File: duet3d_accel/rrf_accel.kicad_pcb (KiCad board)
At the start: 2 copper layers, 118.7 x 50.3 mm, 13 parts, among them J1 Conn_02x05_Odd_Even, U1 LIS3DH

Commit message: Layout in progress.
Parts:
- U1: footprint Package_LGA:LGA-16_3x3mm_P0.5mm_LayoutBorder3x5y -> duet3d_accel:LGA-16_3x3mm_P0.5mm_LayoutBorder3x5y
- moved R4 11.8 mm to (103.8, 99.3)
- moved R6 11.7 mm to (96.1, 99.4)
- moved D1 11.6 mm to (107.1, 100.1)
- moved R5 11.4 mm to (105.9, 99.4)
- moved J1 11.1 mm to (100.0, 93.3)
- moved U1 11.0 mm to (100.0, 100.0)
- moved R1 10.9 mm to (95.1, 99.3)
- moved R3 10.8 mm to (105.2, 101.3)
- moved R2 10.8 mm to (104.8, 99.4)
- moved C2 10.8 mm to (102.4, 100.7)
- moved C3 10.7 mm to (93.8, 99.9)
- moved C1 10.7 mm to (92.2, 99.9)
- moved C4 10.5 mm to (97.3, 99.9)
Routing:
- net /MOSI: track 22.4 -> 26.0 mm
- net Net-(U1-SDA/SDI/SDO): track 6.61 -> 3.88 mm
- net +3V3: track 23.5 -> 25.2 mm
- net Net-(U1-CS): track 2.79 -> 4.40 mm
- net Net-(U1-SCL/SPC): track 6.54 -> 5.48 mm
- net /SCK: track 5.43 -> 4.53 mm
- net Net-(D1-A): track 2.32 -> 1.47 mm
- net /CS: track 14.1 -> 14.8 mm
- net /INT: track 15.0 -> 14.5 mm
- net GNDD: track 16.6 -> 16.4 mm, vias 9 -> 8
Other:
- board size 118.7 x 50.3 mm -> 100 x 100 mm

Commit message: More layout.
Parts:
- moved C1 138.3 mm to (-7.76, 4.40)
- moved C2 138.3 mm to (2.43, 5.19)
- moved C3 138.3 mm to (-6.23, 4.40)
- moved C4 138.3 mm to (-2.65, 4.40)
- moved D1 138.3 mm to (7.13, 4.55)
- moved J1 138.3 mm to (0.00, -2.20)
- moved R1 138.3 mm to (-4.94, 3.84)
- moved R2 138.3 mm to (4.84, 3.87)
- moved R3 138.3 mm to (5.22, 5.82)
- moved R4 138.3 mm to (3.83, 3.84)
- moved R5 138.3 mm to (5.86, 3.87)
- moved R6 138.3 mm to (-3.92, 3.86)
- moved U1 138.3 mm to (0.00, 4.50)
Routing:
- net /MOSI: track 26.0 -> 28.2 mm
- net /SCK: track 4.53 -> 3.49 mm
- net /CS: track 14.8 -> 15.8 mm
- net /MISO: track 5.99 -> 5.06 mm
- net /INT: track 14.5 -> 15.2 mm
- net GNDD: track 16.4 -> 15.8 mm
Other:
- board text added: "1"
- board text added: "LIS3DH"

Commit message: Tweaked the layout
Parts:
- moved C4 0.35 mm to (-3.00, 4.40)
- moved R6 0.30 mm to (-4.22, 3.86)
- moved R1 0.25 mm to (-5.18, 3.86)
- moved C1 0.17 mm to (-7.92, 4.40)
- moved C3 0.17 mm to (-6.40, 4.40)
- moved C2 0.16 mm to (2.59, 5.18)
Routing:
- net +3V3: track 25.3 -> 28.8 mm
- net /CS: track 15.8 -> 14.7 mm
- net GNDD: track 15.8 -> 14.9 mm, vias 8 -> 5
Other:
- outline, holes or cut-outs redrawn

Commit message: Renamed libraries
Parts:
- J1: footprint duet3d_accel:PinHeader_2x05_P2.54mm_Vertical_SMD -> rrf_accel:PinHeader_2x05_P2.54mm_Vertical_SMD
- U1: footprint duet3d_accel:LGA-16_3x3mm_P0.5mm_LayoutBorder3x5y -> rrf_accel:LGA-16_3x3mm_P0.5mm_LayoutBorder3x5y
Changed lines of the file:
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@@
     )
   )
-  (footprint "duet3d_accel:PinHeader_2x05_P2.54mm_Vertical_SMD" (layer "F.Cu")
+  (footprint "rrf_accel:PinHeader_2x05_P2.54mm_Vertical_SMD" (layer "F.Cu")
     (at 0 -2.2 -90)
     (descr "surface-mounted straight pin header, 2x05, 2.54mm pitch, double rows")
@@
     (property "ki_description" "Generic connector, double row, 02x05, odd/even pin numbering scheme (row 1 odd numbers, row 2 even numbers), script generated (kicad-library-utils/schlib/autogen/connector/)")
     (property "ki_keywords" "connector")
-    (fp_text reference "J1" (at 0 -7.41 90) (layer "F.SilkS") hide
-        (effects (font (size 1 1) (thickness 0.15)))
-    )
-    (fp_text value "Conn_02x05_Odd_Even" (at 0 7.41 90) (layer "F.Fab") hide
+    (fp_text reference "J1" (at 0 -7.41 -90) (layer "F.SilkS") hide
+        (effects (font (size 1 1) (thickness 0.15)))
+    )
+    (fp_text value "Conn_02x05_Odd_Even" (at 0 7.41 -90) (layer "F.Fab") hide
         (effects (font (size 1 1) (thickness 0.15)))
     )
@@
     )
   )
-  (footprint "duet3d_accel:LGA-16_3x3mm_P0.5mm_LayoutBorder3x5y" (layer "F.Cu")
+  (footprint "rrf_accel:LGA-16_3x3mm_P0.5mm_LayoutBorder3x5y" (layer "F.Cu")
     (at 0 4.5 180)
     (descr "LGA, 16 Pin (http://www.st.com/resource/en/datasheet/lis331hh.pdf), generated with kicad-footprint-generator ipc_noLead_generator.py")
@@
     (property "ki_keywords" "3-axis accelerometer i2c spi mems")
     (attr smd)
-    (fp_text reference "U1" (at 0 -2.45) (layer "F.SilkS") hide
-        (effects (font (size 1 1) (thickness 0.15)))
-    )
-    (fp_text value "LIS3DH" (at 0 2.45) (layer "F.Fab") hide
-        (effects (font (size 1 1) (thickness 0.15)))
+    (fp_text reference "U1" (at 0 -2.45 180) (layer "F.SilkS") hide
+        (effects (font (size 1 1) (thickness 0.15)))
+    )
+    (fp_text value "LIS3DH" (at 0 2.45 180) (layer "F.Fab") hide
+        (effects (font (size 1 1) (thickness 0.15)))
+    )
+    (fp_text user "${REFERENCE}" (at 0 0 180) (layer "F.Fab")
+        (effects (font (size 0.75 0.75) (thickness 0.11)))
     )
     (fp_line (start -1.61 1.61) (end -1.61 1.435)

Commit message: Fixed schematic.
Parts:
- moved R6 1.58 mm to (-2.64, 3.90)
- moved C4 0.91 mm to (-3.91, 4.42)
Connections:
- C4 pad 1: /CS -> Net-(U1-CS)
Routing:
- net /CS: track 14.7 -> 13.9 mm
- net Net-(U1-CS): track 4.40 -> 5.09 mm
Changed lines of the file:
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@@
       (outputformat 1)
       (mirror false)
-      (drillshape 1)
+      (drillshape 0)
       (scaleselection 1)
       (outputdirectory "")
@@
   (net 19 "unconnected-(U1-INT2-Pad9)")
   (footprint "Resistor_SMD:R_0402_1005Metric_Pad0.72x0.64mm_HandSolder" (layer "F.Cu")
-    (at -4.2164 3.8561 -90)
+    (at -2.6416 3.8995 -90)
     (descr "Resistor SMD 0402 (1005 Metric), square (rectangular) end terminal, IPC_7351 nominal with elongated pad for handsoldering. (Body size source: IPC-SM-782 page 72, https://www.pcb-3d.com/wordpress/wp-content/uploads/ipc-sm-782a_amendment_1_and_2.pdf), generated with kicad-footprint-generator")
     (tags "resistor handsolder")
@@
   )
   (footprint "Capacitor_SMD:C_0603_1608Metric_Pad1.08x0.95mm_HandSolder" (layer "F.Cu")
-    (at -2.9972 4.4005 -90)
+    (at -3.9116 4.4185 -90)
     (descr "Capacitor SMD 0603 (1608 Metric), square (rectangular) end terminal, IPC_7351 nominal with elongated pad for handsoldering. (Body size source: IPC-SM-782 page 76, https://www.pcb-3d.com/wordpress/wp-content/uploads/ipc-sm-782a_amendment_1_and_2.pdf), generated with kicad-footprint-generator")
     (tags "capacitor handsolder")
@@
       (stroke (width 0.1) (type solid)) (layer "F.Fab"))
     (pad "1" smd roundrect (at -0.8625 0 270) (size 1.075 0.95) (layers "F.Cu" "F.Paste" "F.Mask") (roundrect_rratio 0.25)
-      (net 4 "/CS") (pintype "passive"))
+      (net 16 "Net-(U1-CS)") (pintype "passive"))
     (pad "2" smd roundrect (at 0.8625 0 270) (size 1.075 0.95) (layers "F.Cu" "F.Paste" "F.Mask") (roundrect_rratio 0.25)
       (net 2 "GNDD") (pintype "passive"))
@@
   (segment (start 2.5387 4.6723) (end 3.3528 5.4864) (width 0.3048) (layer "F.Cu") (net 2))
   (via (at -7.7808 6.2304) (size 0.762) (drill 0.381) (layers "F.Cu" "B.Cu") (net 2))
-  (via (at -3.9624 5.334) (size 0.762) (drill 0.381) (layers "F.Cu" "B.Cu") (net 2))
-  (via (at -5.5372 5.842) (size 0.762) (drill 0.381) (layers "F.Cu" "B.Cu") (net 2))
+  (via (at -2.8702 5.4102) (size 0.762) (drill 0.381) (layers "F.Cu" "B.Cu") (net 2))
+  (via (at -5.5372 5.6642) (size 0.762) (drill 0.381) (layers "F.Cu" "B.Cu") (net 2))
   (via (at 3.504969 5.6388) (size 0.762) (drill 0.381) (layers "F.Cu" "B.Cu") (net 2))
   (via (at 0 4.5) (size 1.27) (drill 0.635) (layers "F.Cu" "B.Cu") (net 2))
+  (segment (start 2.4808 -3.8016) (end 2.4808 -4.687) (width 0.1524) (layer "F.Cu") (net 3))
+  (segment (start -4.572 2.4892) (end -1.8368 2.4892) (width 0.1524) (layer "F.Cu") (net 3))
   (segment (start -6.2314 3.538) (end -5.9567 3.2633) (width 0.1524) (layer "F.Cu") (net 3))
+  (segment (start -0.7874 -2.667) (end 1.3462 -2.667) (width 0.1524) (layer "F.Cu") (net 3))
+  (segment (start -5.9567 3.2633) (end -5.1816 3.2633) (width 0.1524) (layer "F.Cu") (net 3))
+  (segment (start -1.7272 2.3796) (end -1.7272 -1.7272) (width 0.1524) (layer "F.Cu") (net 3))
+  (segment (start -1.8368 2.4892) (end -1.7272 2.3796) (width 0.1524) (layer "F.Cu") (net 3))
+  (segment (start 1.3462 -2.667) (end 2.4808 -3.8016) (width 0.1524) (layer "F.Cu") (net 3))
   (segment (start -5.1816 3.2633) (end -5.1816 3.0988) (width 0.1524) (layer "F.Cu") (net 3))
-  (segment (start -5.9567 3.2633) (end -5.1816 3.2633) (width 0.1524) (layer "F.Cu") (net 3))
-  (segment (start 2.4808 -3.8016) (end 2.4808 -4.687) (width 0.1524) (layer "F.Cu") (net 3))
-  (segment (start -1.089699 -2.821901) (end 1.501101 -2.821901) (width 0.1524) (layer "F.Cu") (net 3))
-  (segment (start -1.7272 -2.1844) (end -1.089699 -2.821901) (width 0.1524) (layer "F.Cu") (net 3))
-  (segment (start -4.7244 2.6416) (end -2.2362 2.6416) (width 0.1524) (layer "F.Cu") (net 3))
-  (segment (start -5.1816 3.0988) (end -4.7244 2.6416) (width 0.1524) (layer "F.Cu") (net 3))
-  (segment (start -1.7272 2.1326) (end -1.7272 -2.1844) (width 0.1524) (layer "F.Cu") (net 3))
-  (segment (start 1.501101 -2.821901) (end 2.4808 -3.8016) (width 0.1524) (layer "F.Cu") (net 3))
-  (segment (start -2.2362 2.6416) (end -1.7272 2.1326) (width 0.1524) (layer "F.Cu") (net 3))
-  (segment (start -2.267774 3.2) (end -2.54 3.2) (width 0.1524) (layer "F.Cu") (net 4))
-  (segment (start -1.27 2.202226) (end -2.267774 3.2) (width 0.1524) (layer "F.Cu") (net 4))
-  (segment (start -1.27 -1.7272) (end -1.27 2.202226) (width 0.1524) (layer "F.Cu") (net 4))
-  (segment (start -3.92 3.2586) (end -2.9294 3.2586) (width 0.1524) (layer "F.Cu") (net 4))
+  (segment (start -1.7272 -1.7272) (end -0.7874 -2.667) (width 0.1524) (layer "F.Cu") (net 3))
+  (segment (start -5.1816 3.0988) (end -4.572 2.4892) (width 0.1524) (layer "F.Cu") (net 3))
+  (segment (start 5.0208 -3.6492) (end 3.5052 -2.1336) (width 0.1524) (layer "F.Cu") (net 4))
+  (segment (start -0.6096 -2.1336) (end -1.27 -1.4732) (width 0.1524) (layer "F.Cu") (net 4))
+  (segment (start -1.27 -1.4732) (end -1.27 2.5146) (width 0.1524) (layer "F.Cu") (net 4))
   (segment (start 5.0208 -4.687) (end 5.0208 -3.6492) (width 0.1524) (layer "F.Cu") (net 4))
-  (segment (start 5.0208 -3.6492) (end 3.5052 -2.1336) (width 0.1524) (layer "F.Cu") (net 4))
-  (segment (start -0.8636 -2.1336) (end -1.27 -1.7272) (width 0.1524) (layer "F.Cu") (net 4))
-  (segment (start 3.5052 -2.1336) (end -0.8636 -2.1336) (width 0.1524) (layer "F.Cu") (net 4))
+  (segment (start 3.5052 -2.1336) (end -0.6096 -2.1336) (width 0.1524) (layer "F.Cu") (net 4))
+  (segment (start -1.523501 2.768101) (end -2.107701 2.768101) (width 0.1524) (layer "F.Cu") (net 4))
+  (segment (start -2.107701 2.768101) (end -2.6416 3.302) (width 0.1524) (layer "F.Cu") (net 4))
+  (segment (start -1.27 2.5146) (end -1.523501 2.768101) (width 0.1524) (layer "F.Cu") (net 4))
   (segment (start 6.734 5.824) (end 7.129 5.429) (width 0.1524) (layer "F.Cu") (net 5))
   (segment (start 5.8215 5.824) (end 6.734 5.824) (width 0.1524) (layer "F.Cu") (net 5))
@@
   (segment (start 4.843 3.27065) (end 4.755824 3.27065) (width 0.1524) (layer "F.Cu") (net 8))
   (segment (start 3.753174 2.268) (end 1.8108 2.268) (width 0.1524) (layer "F.Cu") (net 8))
-  (segment (start -5.1816 5.1308) (end -5.1816 4.4583) (width 0.1524) (layer "F.Cu") (net 12))
-  (segment (start -1.9642 5.7478) (end -2.2436 6.0272) (width 0.1524) (layer "F.Cu") (net 12))
-  (segment (start -1.7324 4.5) (end -1.9642 4.7318) (width 0.1524) (layer "F.Cu") (net 12))
-  (segment (start -1.9642 4.7318) (end -1.9642 5.7478) (width 0.1524) (layer "F.Cu") (net 12))
-  (segment (start -2.2436 6.0272) (end -4.2852 6.0272) (width 0.1524) (layer "F.Cu") (net 12))
-  (segment (start -1.35 4.5) (end -1.7324 4.5) (width 0.1524) (layer "F.Cu") (net 12))
-  (segment (start -4.2852 6.0272) (end -5.1816 5.1308) (width 0.1524) (layer "F.Cu") (net 12))
+  (segment (start -5.1562 5.1054) (end -5.1562 4.4837) (width 0.1524) (layer "F.Cu") (net 12))
+  (segment (start -1.9642 5.7478) (end -2.3632 6.1468) (width 0.1524) (layer "F.Cu") (net 12))
+  (segment (start -1.9642 4.6312) (end -1.9642 5.7478) (width 0.1524) (layer "F.Cu") (net 12))
+  (segment (start -4.572 6.1468) (end -4.8387 5.8801) (width 0.1524) (layer "F.Cu") (net 12))
+  (segment (start -5.1562 4.4837) (end -5.1816 4.4583) (width 0.1524) (layer "F.Cu") (net 12))
+  (segment (start -4.8387 5.8801) (end -4.8387 5.4229) (width 0.1524) (layer "F.Cu") (net 12))
+  (segment (start -4.8387 5.4229) (end -5.1562 5.1054) (width 0.1524) (layer "F.Cu") (net 12))
+  (segment (start -1.35 4.5) (end -1.833 4.5) (width 0.1524) (layer "F.Cu") (net 12))
+  (segment (start -2.3632 6.1468) (end -4.572 6.1468) (width 0.1524) (layer "F.Cu") (net 12))
+  (segment (start -1.833 4.5) (end -1.9642 4.6312) (width 0.1524) (layer "F.Cu") (net 12))
   (segment (start 0.9652 2.5468) (end 0.0948 2.5468) (width 0.1524) (layer "F.Cu") (net 13))
   (segment (start 3.516558 3.806) (end 2.555358 2.8448) (width 0.1524) (layer "F.Cu") (net 13))
@@
   (segment (start 1.225 4) (end 2.921706 4) (width 0.1524) (layer "F.Cu") (net 15))
   (segment (start 3.1412 4.219494) (end 3.1412 4.65645) (width 0.1524) (layer "F.Cu") (net 15))
+  (segment (start -2.6416 4.497) (end -1.9812 3.8366) (width 0.1524) (layer "F.Cu") (net 16))
+  (segment (start -0.5282 3.1218) (end -0.5 3.15) (width 0.1524) (layer "F.Cu") (net 16))
+  (segment (start -3.8862 3.5814) (end -3.8862 4.2672) (width 0.1524) (layer "F.Cu") (net 16))
+  (segment (start -3.8862 4.2672) (end -3.683 4.4704) (width 0.1524) (layer "F.Cu") (net 16))
+  (segment (start -3.9116 3.556) (end -3.8862 3.5814) (width 0.1524) (layer "F.Cu") (net 16))
+  (segment (start -1.9812 3.8366) (end -1.9812 3.320088) (width 0.1524) (layer "F.Cu") (net 16))
+  (segment (start -1.9812 3.320088) (end -1.782912 3.1218) (width 0.1524) (layer "F.Cu") (net 16))
+  (segment (start -3.683 4.4704) (end -2.6682 4.4704) (width 0.1524) (layer "F.Cu") (net 16))
   (segment (start -1.782912 3.1218) (end -0.5282 3.1218) (width 0.1524) (layer "F.Cu") (net 16))
-  (segment (start -3.92 4.4536) (end -2.404856 4.4536) (width 0.1524) (layer "F.Cu") (net 16))
-  (segment (start -1.9532 3.292088) (end -1.782912 3.1218) (width 0.1524) (layer "F.Cu") (net 16))
-  (segment (start -2.404856 4.4536) (end -1.9532 4.001944) (width 0.1524) (layer "F.Cu") (net 16))
-  (segment (start -1.9532 4.001944) (end -1.9532 3.292088) (width 0.1524) (layer "F.Cu") (net 16))
-  (segment (start -0.5282 3.1218) (end -0.5 3.15) (width 0.1524) (layer "F.Cu") (net 16))
+  (segment (start -2.6682 4.4704) (end -2.6416 4.497) (width 0.1524) (layer "F.Cu") (net 16))
   (zone (net 2) (net_name "GNDD") (layer "B.Cu") (hatch edge 0.5)
     (connect_pads (clearance 0.5))

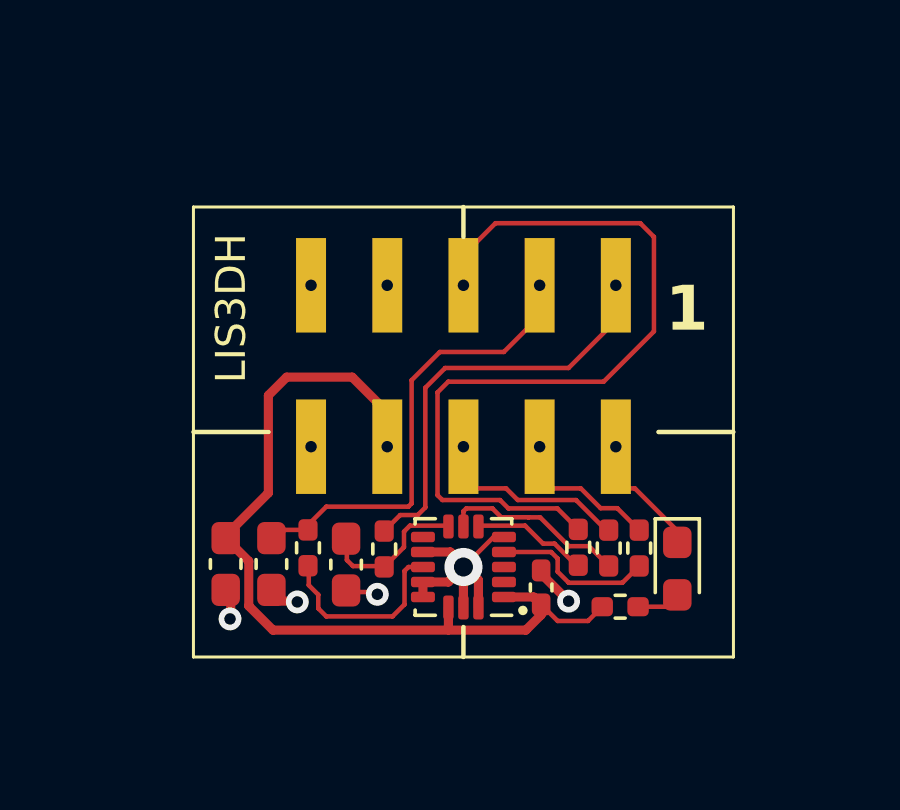
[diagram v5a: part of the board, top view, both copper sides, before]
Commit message: Tweaked schematic and layout.
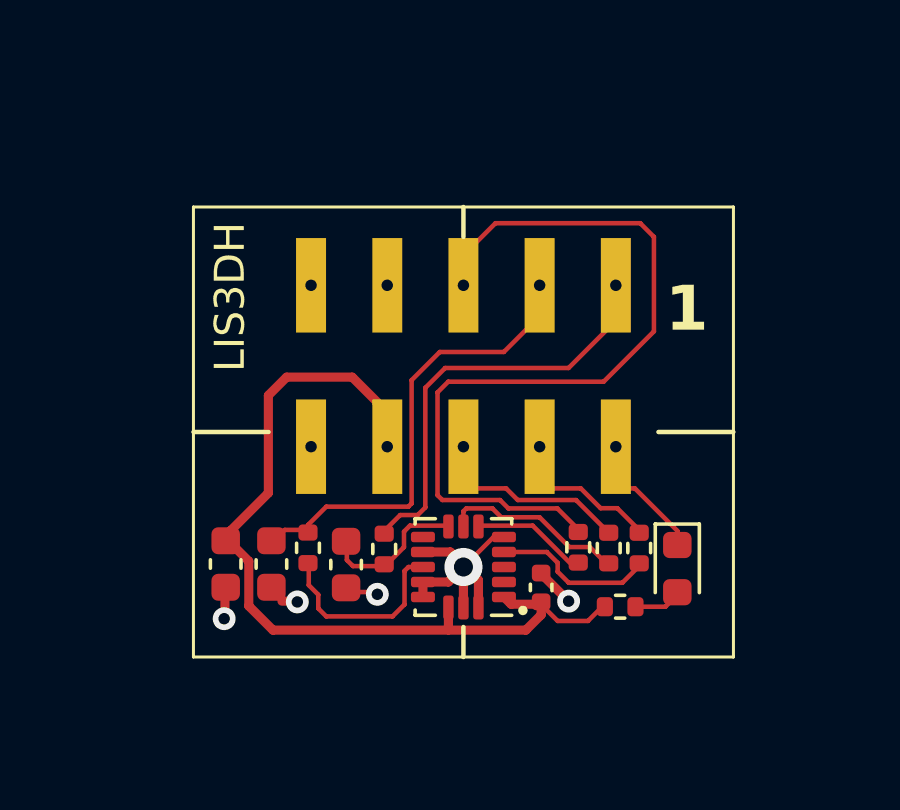
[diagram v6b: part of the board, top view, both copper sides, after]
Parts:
- C1, C3, C4: footprint Capacitor_SMD:C_0603_1608Metric_Pad1.08x0.95mm_HandSolder -> Capacitor_SMD:C_0603_1608Metric
- C2: footprint Capacitor_SMD:C_0402_1005Metric_Pad0.74x0.62mm_HandSolder -> Capacitor_SMD:C_0402_1005Metric
- D1: footprint LED_SMD:LED_0603_1608Metric_Pad1.05x0.95mm_HandSolder -> LED_SMD:LED_0603_1608Metric
- R1, R2, R3, R4, R5, R6: footprint Resistor_SMD:R_0402_1005Metric_Pad0.72x0.64mm_HandSolder -> Resistor_SMD:R_0402_1005Metric
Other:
- board text added: "V0.1"
